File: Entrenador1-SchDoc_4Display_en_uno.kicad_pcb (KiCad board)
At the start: 2 copper layers, 154.9 x 106.7 mm, 85 parts, among them J11 CON8, J3 ICSP, J5 CON8, J6 CON8, J7 CON8, J9 3vias, P1 CONN_01X04, P10 CONN_01X04, P2 CONN_01X04, P3 CONN_01X05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

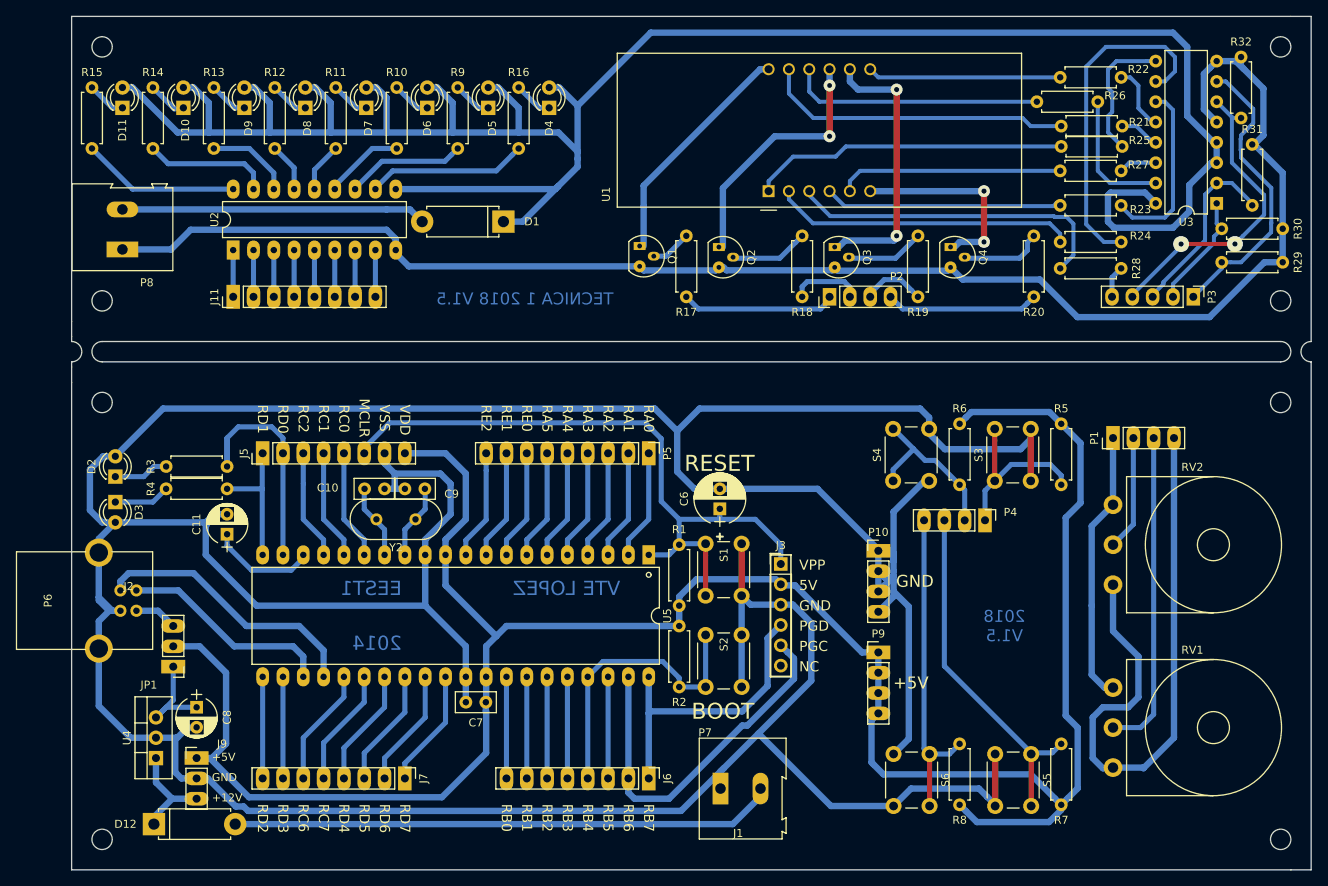
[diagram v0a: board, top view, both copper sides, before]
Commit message: Se modifica el conector USB para un mejor trabajo de los chicos
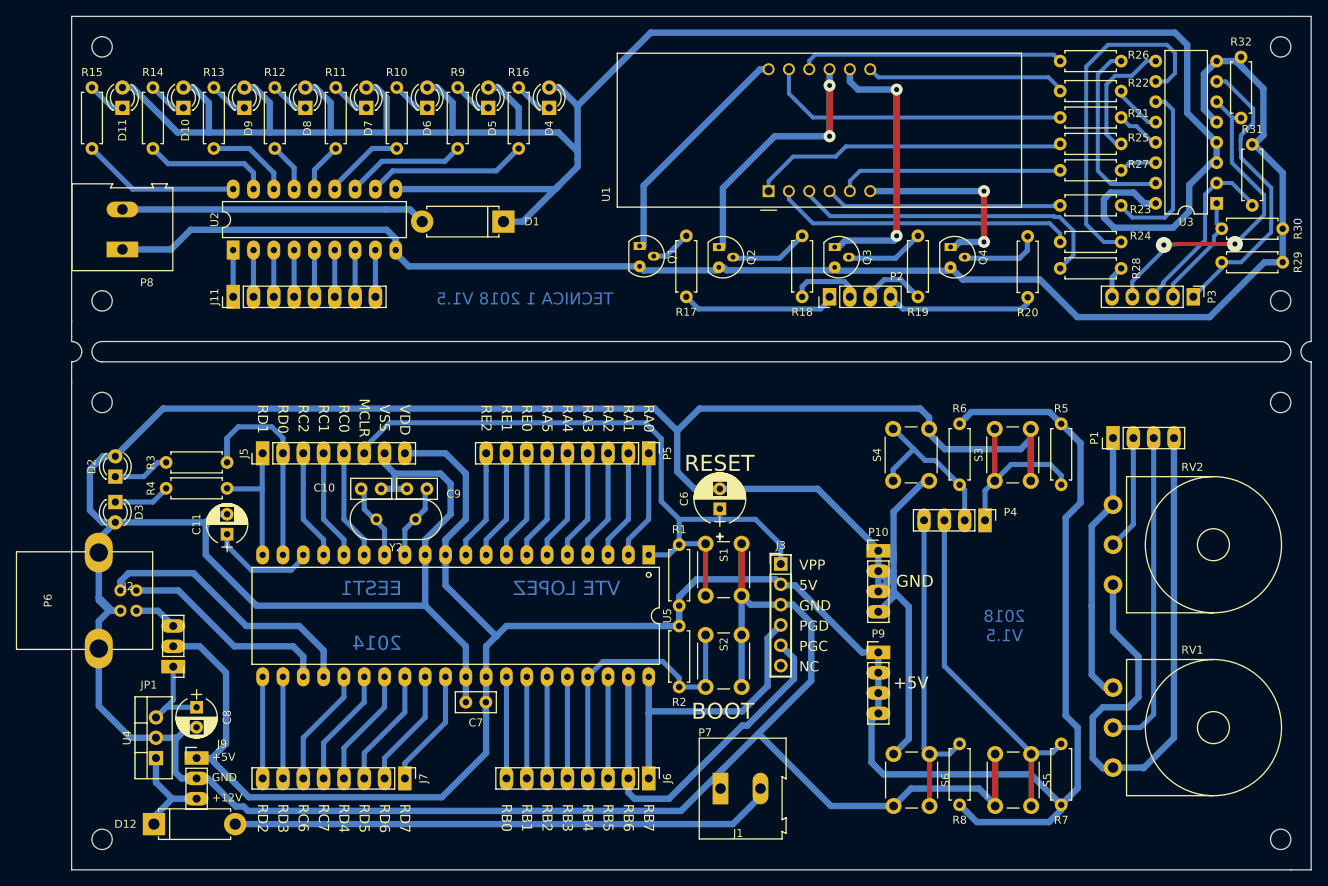
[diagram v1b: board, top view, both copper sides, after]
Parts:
- moved R26 5.86 mm to (197.2, 38.6)
- moved R22 1.71 mm to (197.2, 42.4)
- moved R21 1.09 mm to (197.2, 45.7)
- moved R20 0.76 mm to (185.5, 68.1)
- moved R3 0.51 mm to (77.9, 88.8)
- moved C10 0.42 mm to (102.2, 92.1)
- moved R25 0.34 mm to (197.2, 49.0)
- moved C9 0.25 mm to (110.5, 92.1)
- moved R4 0.06 mm to (77.9, 92.0)
- moved R27 0.06 mm to (197.2, 52.3)
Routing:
- net Net-(R26-Pad1): track 17.0 -> 24.2 mm
- net Net-(R22-Pad1): track 8.31 -> 5.71 mm
- net /b: track 24.2 -> 25.5 mm
- net /f: track 31.8 -> 33.1 mm
- net Net-(R25-Pad1): track 17.2 -> 15.9 mm
- net /Display_D: track 38.7 -> 39.9 mm
- net Net-(R24-Pad1): track 42.1 -> 42.8 mm
- net Net-(R21-Pad1): track 5.03 -> 5.61 mm
- net /a: track 38.8 -> 38.2 mm
- net /h: track 41.3 -> 40.8 mm
- net RD0: track 30.1 -> 29.6 mm

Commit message: Actualización de la placa con nuevos componentes
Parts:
- P6: footprint USB_B -> libreria:USB_B
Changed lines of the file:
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@@
     (add_net "Net-(R27-Pad1)")
   )
-  (module USB_B (layer F.Cu)
+  (module libreria:USB_B (layer F.Cu)
     (at 74.136 107.315 180)
     (descr "USB B connector")
@@
     (fp_line (start 14.99 -4.83) (end 14.99 7.37) (layer F.SilkS) (width 0.12))
     (fp_line (start -2.03 7.37) (end -2.03 -4.83) (layer F.SilkS) (width 0.12))
-    (pad 2 thru_hole circle (at 0 2.54 90) (size 1.52 1.52) (drill 0.81) (layers *.Cu *.Mask)
+    (pad 2 thru_hole oval (at 0 2.54 90) (size 2 1.6) (drill 0.81) (layers *.Cu *.Mask)
       (net 96 RC4))
-    (pad 1 thru_hole circle (at 0 0 90) (size 1.52 1.52) (drill 0.81) (layers *.Cu *.Mask)
+    (pad 1 thru_hole oval (at 0 0 90) (size 2 1.6) (drill 0.81) (layers *.Cu *.Mask)
       (net 31 +5VUSB))
-    (pad 4 thru_hole circle (at 2 0 90) (size 1.52 1.52) (drill 0.81) (layers *.Cu *.Mask)
+    (pad 4 thru_hole oval (at 2 0 90) (size 2 1.6) (drill 0.81) (layers *.Cu *.Mask)
       (net 12 GND))
-    (pad 3 thru_hole circle (at 2 2.54 90) (size 1.52 1.52) (drill 0.81) (layers *.Cu *.Mask)
+    (pad 3 thru_hole oval (at 2 2.54 90) (size 2 1.6) (drill 0.81) (layers *.Cu *.Mask)
       (net 97 RC5))
-    (pad 5 thru_hole oval (at 4.7 7.27 90) (size 5 3.5) (drill 2.3) (layers *.Cu *.Mask)
+    (pad 5 thru_hole oval (at 4.7 7.27 90) (size 5 4) (drill 2.3) (layers *.Cu *.Mask)
       (net 12 GND))
-    (pad 5 thru_hole oval (at 4.7 -4.73 90) (size 5 3.5) (drill 2.3) (layers *.Cu *.Mask)
+    (pad 5 thru_hole oval (at 4.7 -4.73 90) (size 5 4) (drill 2.3) (layers *.Cu *.Mask)
       (net 12 GND))
     (model C:/Users/Admin/Dropbox/tecnica1/Entrenador4to2018/Modelos3d/usb_B.wrl

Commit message: modified:   Entrenador1-SchDoc-cache.lib 	modified:   Entrenador1-SchDoc-rescue.lib 	modified:   Entrenador1-SchDoc.bak 	modified:   Entrenador1-SchDoc.net 	modified:   Entrenador1-SchDoc.pro 	modified:   Entrenador1-SchDoc.sch 	new file:   Entrenador1-SchDoc_4Display_en_uno-cache.lib 	new file:   Entrenador1-SchDoc_4Display_en_uno.bak 	modified:   Entrenador1-SchDoc_4Display_en_uno.kicad_pcb 	modified:   Entrenador1-SchDoc_4Display_en_uno.kicad_pcb-bak 	new file:   Entrenador1-SchDoc_4Display_en_uno.net 	modified:   Entrenador1-SchDoc_4Display_en_uno.pro 	new file:   Entrenador1-SchDoc_4Display_en_uno.sch 	new file:   libreria.pretty/CA56-12EWA.kicad_mod 	modified:   libreria.pretty/TO-92_Molded_Narrow.kicad_mod 	new file:   libreria.pretty/TerminalBlock_bornier-2_P5.08mm.kicad_mod 	new file:   rescue-backup/Entrenador1-SchDoc-2019-06-22-08-57-40.pro 	new file:   rescue-backup/Entrenador1-SchDoc-2019-06-22-08-57-40.sch 	new file:   rescue-backup/Entrenador1-SchDoc-cache-2019-06-22-08-57-40.lib 	new file:   rescue-backup/Entrenador1-SchDoc-rescue-2019-06-22-08-57-40.lib 	new file:   sym-lib-table
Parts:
- P3: footprint libreria:Socket_Strip_Straight_1x05_Pitch2.54mm -> Socket_Strips:Socket_Strip_Straight_1x05_Pitch2.54mm
- P7, P8: footprint libreria:TerminalBlock_Altech_AK300-2_P5.00mm -> Terminal_Blocks:TerminalBlock_bornier-2_P5.08mm
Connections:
- U3 pad 16: VDD -> Vdd
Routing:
- net Net-(Q2-Pad2): track 9.86 -> 8.67 mm
- net Net-(Q4-Pad2): track 10.1 -> 8.99 mm
- net Net-(Q3-Pad2): track 9.85 -> 8.78 mm
- net Net-(Q1-Pad2): track 5.12 -> 4.05 mm
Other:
- board text removed: "2018 V1.5"

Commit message: modified:   Entrenador1-SchDoc_4Display_en_uno.bak 	modified:   Entrenador1-SchDoc_4Display_en_uno.kicad_pcb 	modified:   Entrenador1-SchDoc_4Display_en_uno.kicad_pcb-bak 	modified:   Entrenador1-SchDoc_4Display_en_uno.net 	modified:   Entrenador1-SchDoc_4Display_en_uno.sch 	modified:   libreria.pretty/CA56-12EWA.kicad_mod 	modified:   libreria.pretty/TerminalBlock_bornier-2_P5.08mm.kicad_mod
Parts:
- P3: footprint Socket_Strips:Socket_Strip_Straight_1x05_Pitch2.54mm -> libreria:Socket_Strip_Straight_1x05_Pitch2.54mm
- P7, P8: footprint Terminal_Blocks:TerminalBlock_bornier-2_P5.08mm -> libreria:TerminalBlock_bornier-2_P5.08mm
- U1: footprint Displays_7-Segment:CA56-12EWA -> libreria:CA56-12EWA
- moved R24 0.76 mm to (196.5, 61.2)
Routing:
- net /f: track 33.1 -> 33.8 mm
- net /b: track 25.5 -> 24.9 mm
- net Net-(C8-Pad1): track 12.9 -> 13.5 mm
- net Net-(R24-Pad1): track 42.8 -> 42.3 mm

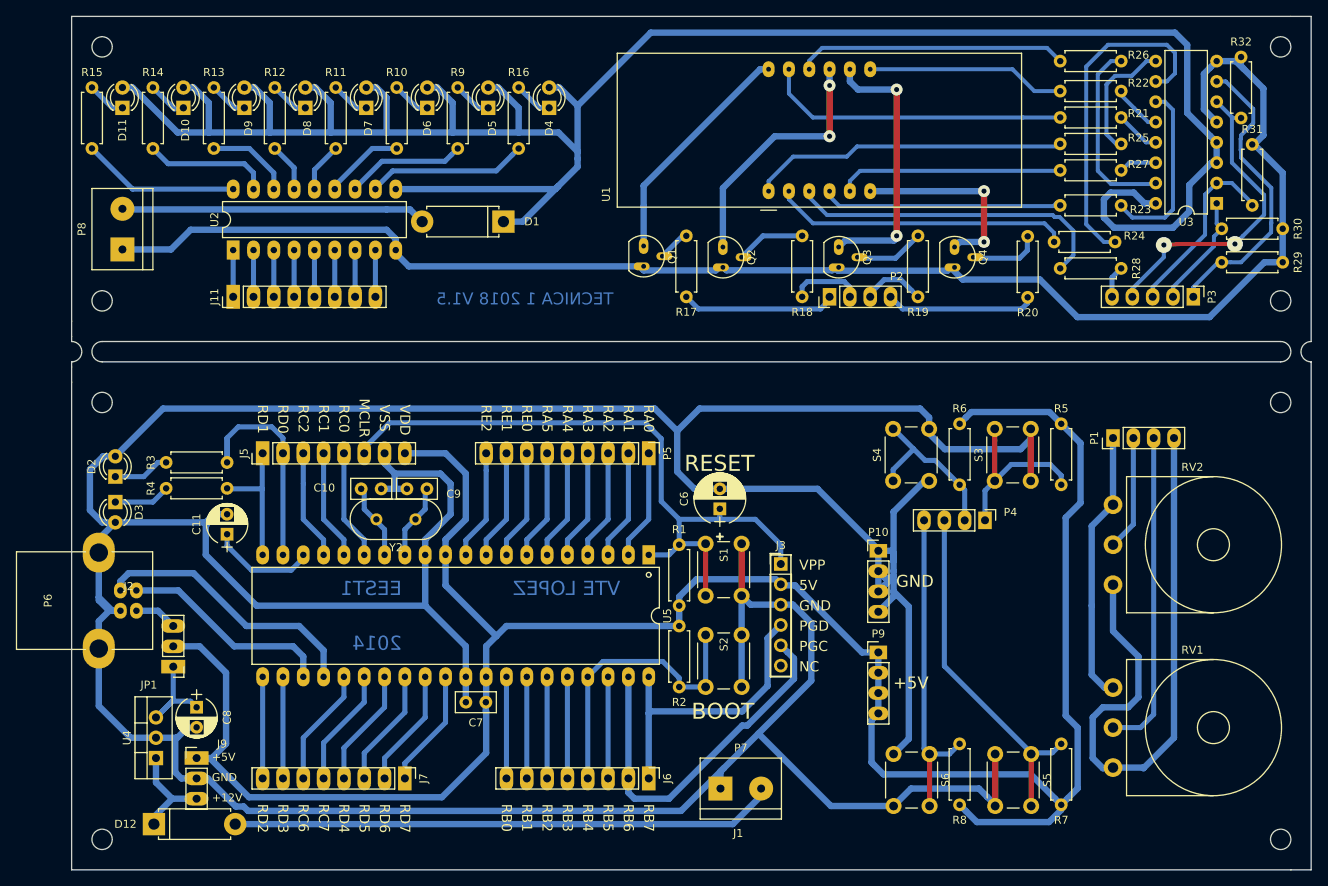
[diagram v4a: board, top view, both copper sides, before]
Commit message: modified:   Entrenador1-SchDoc_4Display_en_uno-cache.lib 	modified:   Entrenador1-SchDoc_4Display_en_uno.bak 	modified:   Entrenador1-SchDoc_4Display_en_uno.kicad_pcb 	modified:   Entrenador1-SchDoc_4Display_en_uno.kicad_pcb-bak 	modified:   Entrenador1-SchDoc_4Display_en_uno.net 	modified:   Entrenador1-SchDoc_4Display_en_uno.sch 	modified:   libreria.pretty/TerminalBlock_bornier-2_P5.08mm.kicad_mod
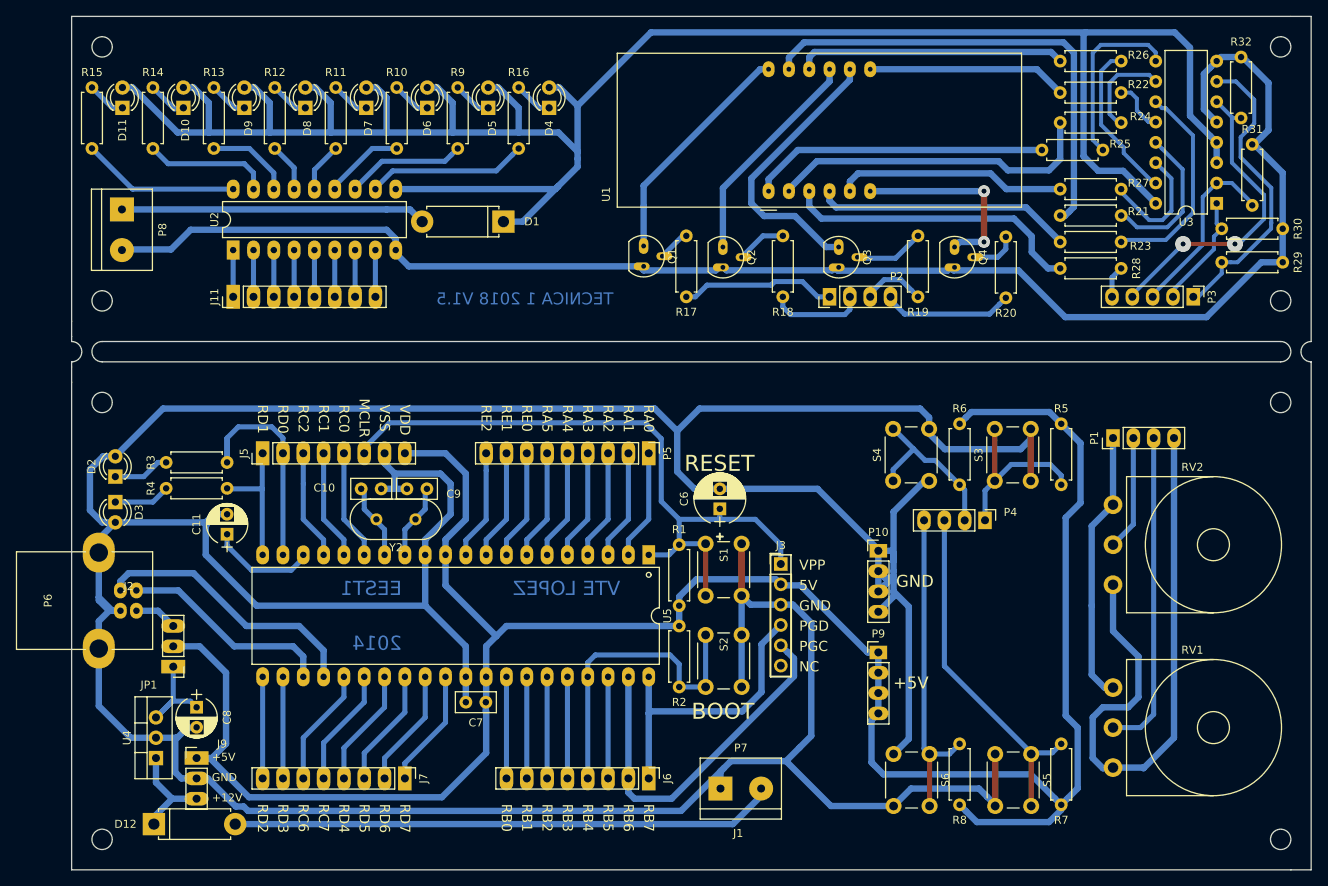
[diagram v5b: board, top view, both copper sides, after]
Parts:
- moved R24 14.9 mm to (197.2, 46.3)
- moved R21 12.3 mm to (197.2, 57.9)
- moved P8 5.00 mm to (72.3, 57.1), turned to 270 degrees
- moved R23 4.57 mm to (197.2, 61.2)
- moved R20 2.73 mm to (182.8, 68.2)
- moved R18 2.41 mm to (154.9, 68.1)
- moved R25 2.41 mm to (194.9, 49.7)
- moved R27 2.35 mm to (197.2, 54.6)
- moved R22 0.19 mm to (197.2, 42.5)
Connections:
- D1 pad 1: VDD -> +5VD
- D10 pad 2: VDD -> +5VD
- D11 pad 2: VDD -> +5VD
- D4 pad 2: VDD -> +5VD
- D5 pad 2: VDD -> +5VD
- D6 pad 2: VDD -> +5VD
- D7 pad 2: VDD -> +5VD
- D8 pad 2: VDD -> +5VD
- D9 pad 2: VDD -> +5VD
- P8 pad 1: GND -> +5VFuente
- P8 pad 2: +5VFuente -> GNDD
- Q1 pad 3: GND -> GNDD
- Q2 pad 3: GND -> GNDD
- Q3 pad 3: GND -> GNDD
- Q4 pad 3: GND -> GNDD
- R29 pad 1: GND -> GNDD
- R30 pad 1: GND -> GNDD
- R31 pad 1: GND -> GNDD
- R32 pad 1: GND -> GNDD
- U2 pad 10: VDD -> +5VD
- U2 pad 9: GND -> GNDD
- U3 pad 16: Vdd -> +5VD
- U3 pad 3: VDD -> +5VD
- U3 pad 4: VDD -> +5VD
- U3 pad 5: GND -> GNDD
- U3 pad 8: GND -> GNDD
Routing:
- net VDD: track 563.4 -> 285.9 mm
- net +5VD: track 0.00 -> 275.0 mm
- net GND: track 740.5 -> 541.2 mm
- net GNDD: track 0.00 -> 197.6 mm
- net Net-(R24-Pad1): track 42.3 -> 12.3 mm
- net /a: track 38.2 -> 59.9 mm
- net Net-(R21-Pad1): track 5.61 -> 19.4 mm
- net Net-(R27-Pad1): track 4.74 -> 15.1 mm
- net Net-(R25-Pad1): track 15.9 -> 22.4 mm
- net /d: track 37.0 -> 41.2 mm
- net Net-(R26-Pad1): track 24.2 -> 20.0 mm
- net /CC2: track 31.8 -> 27.7 mm, vias 2 -> 0
- net Net-(R23-Pad1): track 22.9 -> 26.5 mm
- net /h: track 40.9 -> 37.6 mm
- net Net-(Q4-Pad2): track 8.99 -> 6.02 mm
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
